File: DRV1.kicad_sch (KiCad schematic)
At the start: 15 parts

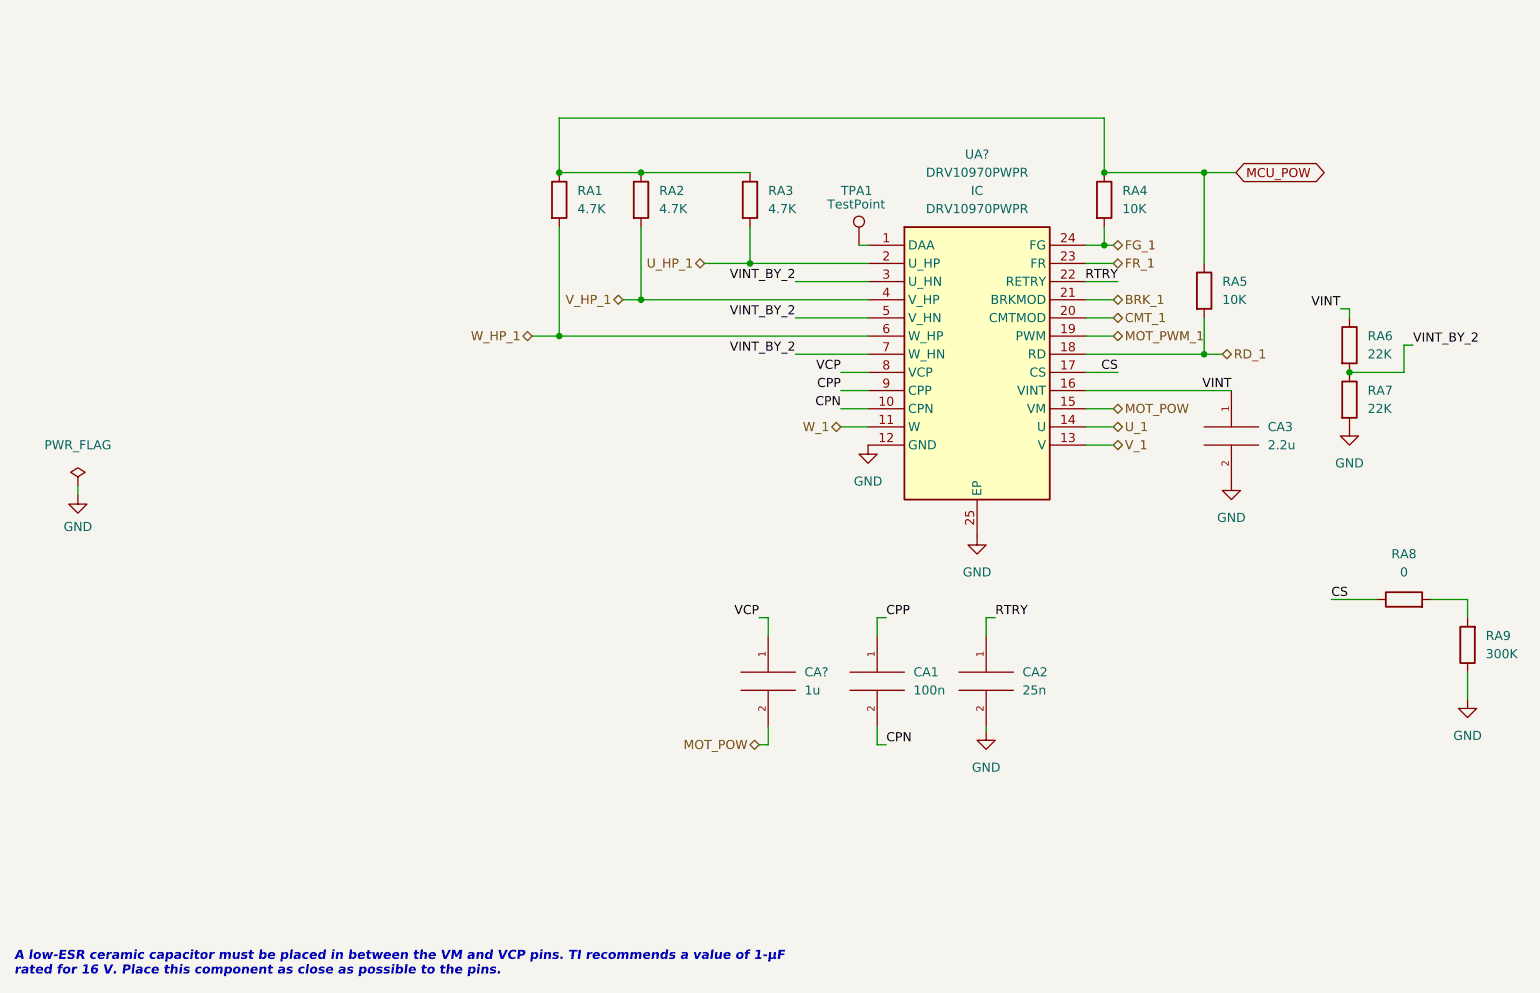
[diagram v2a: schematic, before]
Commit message: Max ERC errors corrected
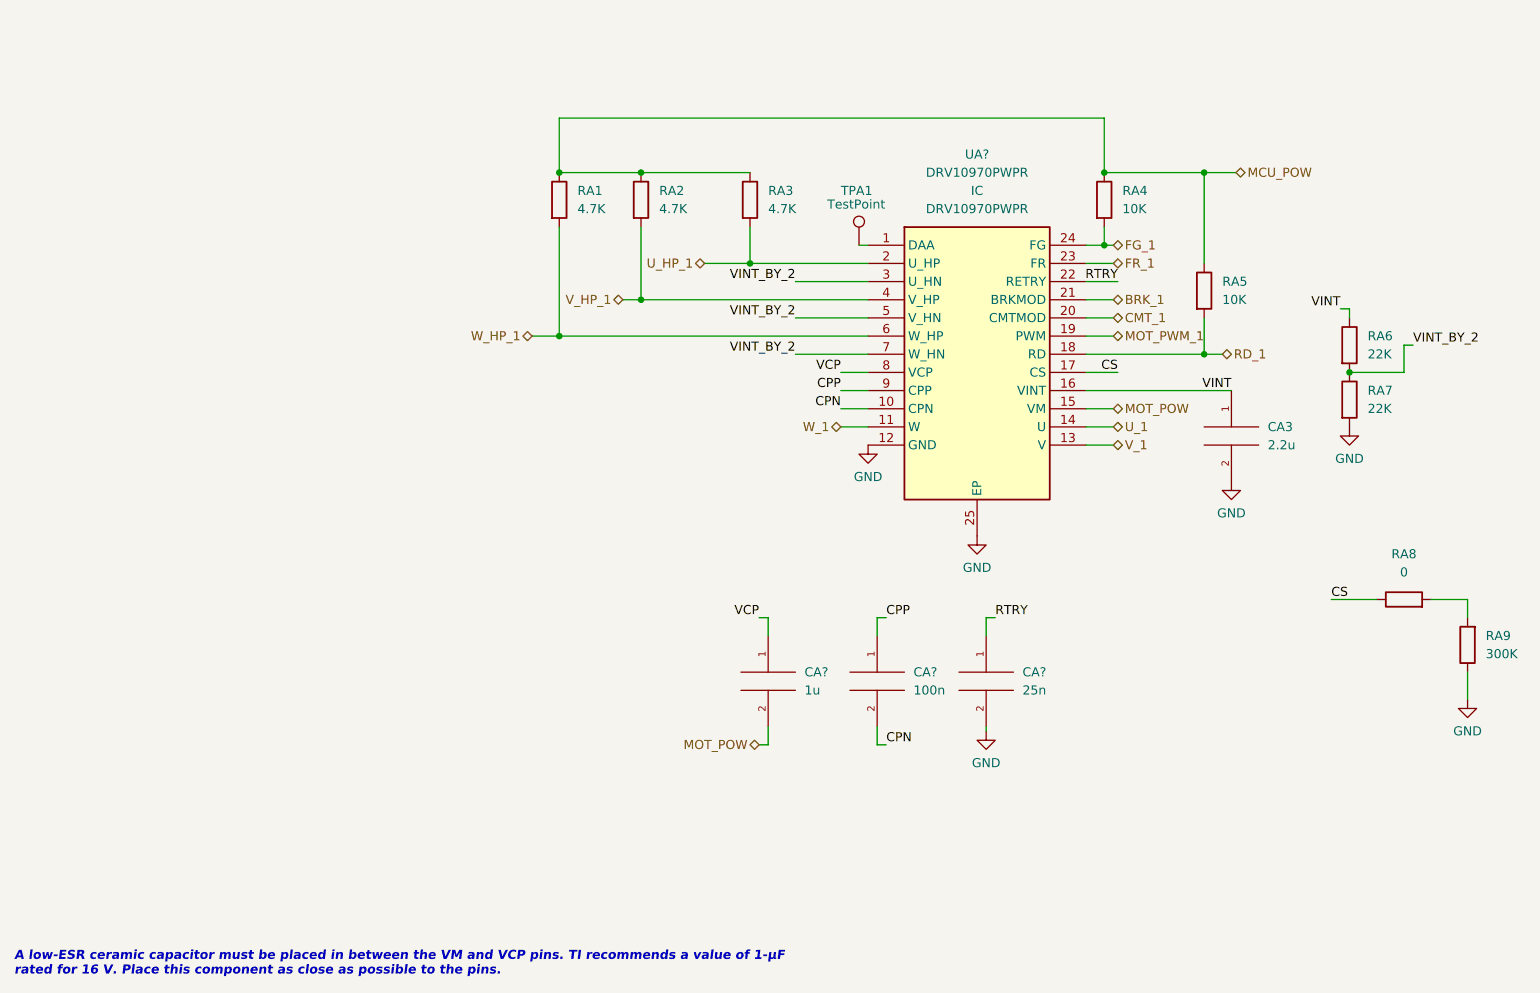
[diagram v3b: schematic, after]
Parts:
- renumbered CA1 to CA?, CA2 to CA?
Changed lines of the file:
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@@
-    (stroke (width 0) (type default) (color 0 0 0 0))
-  )
-  (wire (pts (xy 27.94 121.285) (xy 27.94 120.015))
     (stroke (width 0) (type default) (color 0 0 0 0))
   )
@@
     (effects (font (size 1.27 1.27)) (justify left bottom))
   )
-  (global_label "MCU_POW" (shape bidirectional) (at 189.865 76.2 0) (fields_autoplaced)
-    (effects (font (size 1.27 1.27)) (justify left))
-    (property "Intersheet References" "${INTERSHEET_REFS}" (id 0) (at 201.3495 76.1206 0)
-      (effects (font (size 1.27 1.27)) (justify left) hide)
-    )
-  )
   (hierarchical_label "FR_1" (shape bidirectional) (at 172.72 88.9 0)
     (effects (font (size 1.27 1.27)) (justify left))
@@
     (effects (font (size 1.27 1.27)) (justify right))
   )
+  (hierarchical_label "MCU_POW" (shape bidirectional) (at 189.865 76.2 0)
+    (effects (font (size 1.27 1.27)) (justify left))
+  )
   (hierarchical_label "W_HP_1" (shape bidirectional) (at 91.44 99.06 180)
     (effects (font (size 1.27 1.27)) (justify right))
@@
     (pin "2")
   )
-  (symbol (lib_id "power:GND") (at 154.94 154.305 0) (unit 1)
+  (symbol (lib_id "upsat-comms-hardware:GND") (at 154.94 154.305 0) (unit 1)
     (in_bom yes) (on_board yes) (fields_autoplaced)
     (property "Reference" "#PWR0111" (id 0) (at 154.94 160.655 0)
       (effects (font (size 1.27 1.27)) hide)
     )
-    (property "Value" "GND" (id 1) (at 154.94 159.385 0))
-    (property "Footprint" "" (id 2) (at 154.94 154.305 0)
-      (effects (font (size 1.27 1.27)) hide)
-    )
-    (property "Datasheet" "" (id 3) (at 154.94 154.305 0)
-      (effects (font (size 1.27 1.27)) hide)
-    )
+    (property "Value" "GND" (id 1) (at 154.94 158.75 0))
+    (property "Footprint" "" (id 2) (at 154.94 154.305 0))
+    (property "Datasheet" "" (id 3) (at 154.94 154.305 0))
     (pin "1")
   )
@@
     (pin "2")
   )
-  (symbol (lib_id "power:GND") (at 205.74 111.76 0) (unit 1)
-    (in_bom yes) (on_board yes) (fields_autoplaced)
-    (property "Reference" "#PWR0114" (id 0) (at 205.74 118.11 0)
-      (effects (font (size 1.27 1.27)) hide)
-    )
-    (property "Value" "GND" (id 1) (at 205.74 116.84 0))
-    (property "Footprint" "" (id 2) (at 205.74 111.76 0)
-      (effects (font (size 1.27 1.27)) hide)
-    )
-    (property "Datasheet" "" (id 3) (at 205.74 111.76 0)
-      (effects (font (size 1.27 1.27)) hide)
-    )
-    (pin "1")
-  )
-  (symbol (lib_id "power:GND") (at 222.25 149.86 0) (unit 1)
-    (in_bom yes) (on_board yes) (fields_autoplaced)
-    (property "Reference" "#PWR0112" (id 0) (at 222.25 156.21 0)
-      (effects (font (size 1.27 1.27)) hide)
-    )
-    (property "Value" "GND" (id 1) (at 222.25 154.94 0))
-    (property "Footprint" "" (id 2) (at 222.25 149.86 0)
-      (effects (font (size 1.27 1.27)) hide)
-    )
-    (property "Datasheet" "" (id 3) (at 222.25 149.86 0)
-      (effects (font (size 1.27 1.27)) hide)
-    )
-    (pin "1")
-  )
   (symbol (lib_id "pspice:C") (at 139.7 147.32 0) (unit 1)
     (in_bom yes) (on_board yes) (fields_autoplaced)
-    (property "Reference" "CA1" (id 0) (at 144.78 146.0499 0)
+    (property "Reference" "CA?" (id 0) (at 144.78 146.0499 0)
       (effects (font (size 1.27 1.27)) (justify left))
     )
@@
   (symbol (lib_id "pspice:C") (at 154.94 147.32 0) (unit 1)
     (in_bom yes) (on_board yes) (fields_autoplaced)
-    (property "Reference" "CA2" (id 0) (at 160.02 146.0499 0)
+    (property "Reference" "CA?" (id 0) (at 160.02 146.0499 0)
       (effects (font (size 1.27 1.27)) (justify left))
     )
@@
     (pin "2")
   )
-  (symbol (lib_id "power:GND") (at 27.94 121.285 0) (unit 1)
-    (in_bom yes) (on_board yes) (fields_autoplaced)
-    (property "Reference" "#PWR0267" (id 0) (at 27.94 127.635 0)
-      (effects (font (size 1.27 1.27)) hide)
-    )
-    (property "Value" "GND" (id 1) (at 27.94 125.73 0))
-    (property "Footprint" "" (id 2) (at 27.94 121.285 0)
-      (effects (font (size 1.27 1.27)) hide)
-    )
-    (property "Datasheet" "" (id 3) (at 27.94 121.285 0)
-      (effects (font (size 1.27 1.27)) hide)
-    )
-    (pin "1")
-  )
-  (symbol (lib_id "power:GND") (at 138.43 114.3 0) (unit 1)
+  (symbol (lib_id "upsat-comms-hardware:GND") (at 138.43 114.3 0) (unit 1)
     (in_bom yes) (on_board yes) (fields_autoplaced)
     (property "Reference" "#PWR0109" (id 0) (at 138.43 120.65 0)
       (effects (font (size 1.27 1.27)) hide)
     )
-    (property "Value" "GND" (id 1) (at 138.43 119.38 0))
-    (property "Footprint" "" (id 2) (at 138.43 114.3 0)
-      (effects (font (size 1.27 1.27)) hide)
-    )
-    (property "Datasheet" "" (id 3) (at 138.43 114.3 0)
-      (effects (font (size 1.27 1.27)) hide)
-    )
-    (pin "1")
-  )
-  (symbol (lib_id "power:GND") (at 189.23 119.38 0) (unit 1)
-    (in_bom yes) (on_board yes) (fields_autoplaced)
-    (property "Reference" "#PWR0113" (id 0) (at 189.23 125.73 0)
-      (effects (font (size 1.27 1.27)) hide)
-    )
-    (property "Value" "GND" (id 1) (at 189.23 124.46 0))
-    (property "Footprint" "" (id 2) (at 189.23 119.38 0)
-      (effects (font (size 1.27 1.27)) hide)
-    )
-    (property "Datasheet" "" (id 3) (at 189.23 119.38 0)
-      (effects (font (size 1.27 1.27)) hide)
-    )
+    (property "Value" "GND" (id 1) (at 138.43 118.745 0))
+    (property "Footprint" "" (id 2) (at 138.43 114.3 0))
+    (property "Datasheet" "" (id 3) (at 138.43 114.3 0))
+    (pin "1")
+  )
+  (symbol (lib_id "upsat-comms-hardware:GND") (at 153.67 127 0) (unit 1)
+    (in_bom yes) (on_board yes) (fields_autoplaced)
+    (property "Reference" "#PWR0110" (id 0) (at 153.67 133.35 0)
+      (effects (font (size 1.27 1.27)) hide)
+    )
+    (property "Value" "GND" (id 1) (at 153.67 131.445 0))
+    (property "Footprint" "" (id 2) (at 153.67 127 0))
+    (property "Datasheet" "" (id 3) (at 153.67 127 0))
     (pin "1")
   )
@@
     )
     (property "Datasheet" "~" (id 3) (at 142.24 86.36 0)
-      (effects (font (size 1.27 1.27)) hide)
-    )
-    (pin "1")
-  )
-  (symbol (lib_id "power:GND") (at 153.67 127 0) (unit 1)
-    (in_bom yes) (on_board yes) (fields_autoplaced)
-    (property "Reference" "#PWR0110" (id 0) (at 153.67 133.35 0)
-      (effects (font (size 1.27 1.27)) hide)
-    )
-    (property "Value" "GND" (id 1) (at 153.67 132.08 0))
-    (property "Footprint" "" (id 2) (at 153.67 127 0)
-      (effects (font (size 1.27 1.27)) hide)
-    )
-    (property "Datasheet" "" (id 3) (at 153.67 127 0)
       (effects (font (size 1.27 1.27)) hide)
     )
@@
     (pin "9")
   )
+  (symbol (lib_id "upsat-comms-hardware:GND") (at 222.25 149.86 0) (unit 1)
+    (in_bom yes) (on_board yes) (fields_autoplaced)
+    (property "Reference" "#PWR0112" (id 0) (at 222.25 156.21 0)
+      (effects (font (size 1.27 1.27)) hide)
+    )
+    (property "Value" "GND" (id 1) (at 222.25 154.305 0))
+    (property "Footprint" "" (id 2) (at 222.25 149.86 0))
+    (property "Datasheet" "" (id 3) (at 222.25 149.86 0))
+    (pin "1")
+  )
+  (symbol (lib_id "upsat-comms-hardware:GND") (at 189.23 119.38 0) (unit 1)
+    (in_bom yes) (on_board yes) (fields_autoplaced)
+    (property "Reference" "#PWR0113" (id 0) (at 189.23 125.73 0)
+      (effects (font (size 1.27 1.27)) hide)
+    )
+    (property "Value" "GND" (id 1) (at 189.23 123.825 0))
+    (property "Footprint" "" (id 2) (at 189.23 119.38 0))
+    (property "Datasheet" "" (id 3) (at 189.23 119.38 0))
+    (pin "1")
+  )
   (symbol (lib_id "Device:R") (at 213.36 135.89 90) (unit 1)
     (in_bom yes) (on_board yes) (fields_autoplaced)
@@
     (pin "2")
   )
-  (symbol (lib_id "power:PWR_FLAG") (at 27.94 120.015 0) (unit 1)
-    (in_bom yes) (on_board yes) (fields_autoplaced)
-    (property "Reference" "#FLG0103" (id 0) (at 27.94 118.11 0)
-      (effects (font (size 1.27 1.27)) hide)
-    )
-    (property "Value" "PWR_FLAG" (id 1) (at 27.94 114.3 0))
-    (property "Footprint" "" (id 2) (at 27.94 120.015 0)
-      (effects (font (size 1.27 1.27)) hide)
-    )
-    (property "Datasheet" "~" (id 3) (at 27.94 120.015 0)
-      (effects (font (size 1.27 1.27)) hide)
-    )
-    (pin "1")
-  )
   (symbol (lib_id "Device:R") (at 205.74 107.95 0) (unit 1)
     (in_bom yes) (on_board yes) (fields_autoplaced)
@@
     (pin "2")
   )
+  (symbol (lib_id "upsat-comms-hardware:GND") (at 205.74 111.76 0) (unit 1)
+    (in_bom yes) (on_board yes) (fields_autoplaced)
+    (property "Reference" "#PWR0114" (id 0) (at 205.74 118.11 0)
+      (effects (font (size 1.27 1.27)) hide)
+    )
+    (property "Value" "GND" (id 1) (at 205.74 116.205 0))
+    (property "Footprint" "" (id 2) (at 205.74 111.76 0))
+    (property "Datasheet" "" (id 3) (at 205.74 111.76 0))
+    (pin "1")
+  )
   (symbol (lib_id "Device:R") (at 205.74 100.33 0) (unit 1)

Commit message: Updated the changes
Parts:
- gave numbers to parts that had none: 4
- renumbered CA3 to CA1
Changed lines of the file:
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@@
   (symbol (lib_id "pspice:C") (at 124.46 147.32 0) (unit 1)
     (in_bom yes) (on_board yes) (fields_autoplaced)
-    (property "Reference" "CA?" (id 0) (at 129.54 146.0499 0)
+    (property "Reference" "CA2" (id 0) (at 129.54 146.0499 0)
       (effects (font (size 1.27 1.27)) (justify left))
     )
@@
   (symbol (lib_id "upsat-comms-hardware:GND") (at 154.94 154.305 0) (unit 1)
     (in_bom yes) (on_board yes) (fields_autoplaced)
-    (property "Reference" "#PWR0111" (id 0) (at 154.94 160.655 0)
+    (property "Reference" "#PWR014" (id 0) (at 154.94 160.655 0)
       (effects (font (size 1.27 1.27)) hide)
     )
@@
   (symbol (lib_id "pspice:C") (at 139.7 147.32 0) (unit 1)
     (in_bom yes) (on_board yes) (fields_autoplaced)
-    (property "Reference" "CA?" (id 0) (at 144.78 146.0499 0)
+    (property "Reference" "CA3" (id 0) (at 144.78 146.0499 0)
       (effects (font (size 1.27 1.27)) (justify left))
     )
@@
   (symbol (lib_id "pspice:C") (at 154.94 147.32 0) (unit 1)
     (in_bom yes) (on_board yes) (fields_autoplaced)
-    (property "Reference" "CA?" (id 0) (at 160.02 146.0499 0)
+    (property "Reference" "CA4" (id 0) (at 160.02 146.0499 0)
       (effects (font (size 1.27 1.27)) (justify left))
     )
@@
   (symbol (lib_id "upsat-comms-hardware:GND") (at 138.43 114.3 0) (unit 1)
     (in_bom yes) (on_board yes) (fields_autoplaced)
-    (property "Reference" "#PWR0109" (id 0) (at 138.43 120.65 0)
+    (property "Reference" "#PWR010" (id 0) (at 138.43 120.65 0)
       (effects (font (size 1.27 1.27)) hide)
     )
@@
   (symbol (lib_id "upsat-comms-hardware:GND") (at 153.67 127 0) (unit 1)
     (in_bom yes) (on_board yes) (fields_autoplaced)
-    (property "Reference" "#PWR0110" (id 0) (at 153.67 133.35 0)
+    (property "Reference" "#PWR012" (id 0) (at 153.67 133.35 0)
       (effects (font (size 1.27 1.27)) hide)
     )
@@
   (symbol (lib_id "DRV10970PWPR:DRV10970PWPR") (at 138.43 86.36 0) (unit 1)
     (in_bom yes) (on_board yes) (fields_autoplaced)
-    (property "Reference" "UA?" (id 0) (at 153.67 73.66 0))
+    (property "Reference" "UA1" (id 0) (at 153.67 73.66 0))
     (property "Value" "DRV10970PWPR" (id 1) (at 153.67 76.2 0))
     (property "Footprint" "DRV10970PWPR:SOP65P640X120-25N" (id 2) (at 138.43 86.36 0)
@@
   (symbol (lib_id "upsat-comms-hardware:GND") (at 222.25 149.86 0) (unit 1)
     (in_bom yes) (on_board yes) (fields_autoplaced)
-    (property "Reference" "#PWR0112" (id 0) (at 222.25 156.21 0)
+    (property "Reference" "#PWR013" (id 0) (at 222.25 156.21 0)
       (effects (font (size 1.27 1.27)) hide)
     )
@@
   (symbol (lib_id "upsat-comms-hardware:GND") (at 189.23 119.38 0) (unit 1)
     (in_bom yes) (on_board yes) (fields_autoplaced)
-    (property "Reference" "#PWR0113" (id 0) (at 189.23 125.73 0)
+    (property "Reference" "#PWR011" (id 0) (at 189.23 125.73 0)
       (effects (font (size 1.27 1.27)) hide)
     )
@@
   (symbol (lib_id "pspice:C") (at 189.23 113.03 0) (unit 1)
     (in_bom yes) (on_board yes) (fields_autoplaced)
-    (property "Reference" "CA3" (id 0) (at 194.31 111.7599 0)
+    (property "Reference" "CA1" (id 0) (at 194.31 111.7599 0)
       (effects (font (size 1.27 1.27)) (justify left))
     )
@@
   (symbol (lib_id "upsat-comms-hardware:GND") (at 205.74 111.76 0) (unit 1)
     (in_bom yes) (on_board yes) (fields_autoplaced)
-    (property "Reference" "#PWR0114" (id 0) (at 205.74 118.11 0)
-      (effects (font (size 1.27 1.27)) hide)
-    )
+    (property "Reference" "#PWR09" (id 0) (at 205.74 118.11 0)
+      (effects (font (size 1.27 1.27)) hide)
+    )
